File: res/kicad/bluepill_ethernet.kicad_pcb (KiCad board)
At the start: 2 copper layers, 50.4 x 50.4 mm, 47 parts, among them J1 HEADER-1x20, J2 Conn_01x03, J3 Conn_02x05_Odd_Even, J4 HEADER-1x20, J5 Conn_02x02_Odd_Even, J7 Conn_02x04_Odd_Even, SW1 SW_Push, U1 BluePill_STM32F103C, U2 93C46, U3 WIZ850io, U4 93C46, U5 PCF8574A, U6 LM75B

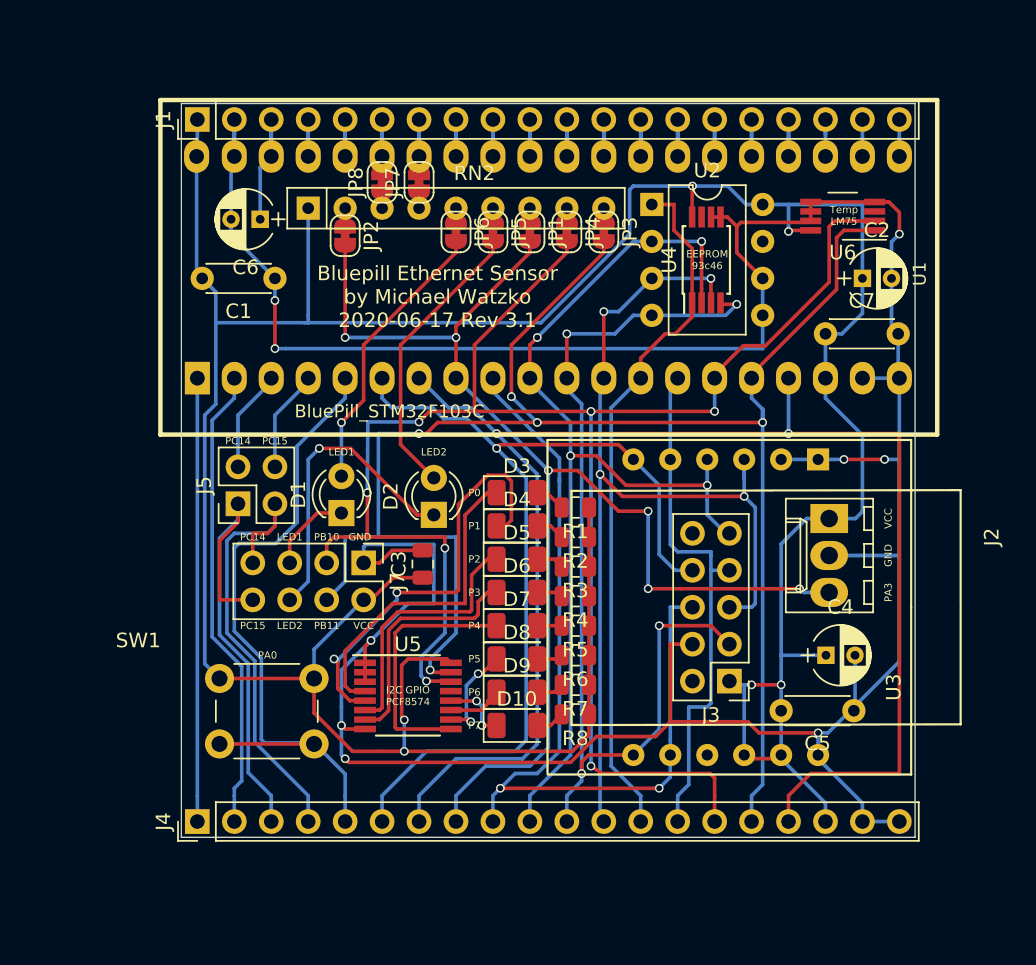
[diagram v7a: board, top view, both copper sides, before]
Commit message: Replace TSSOP packages with SOIC packages
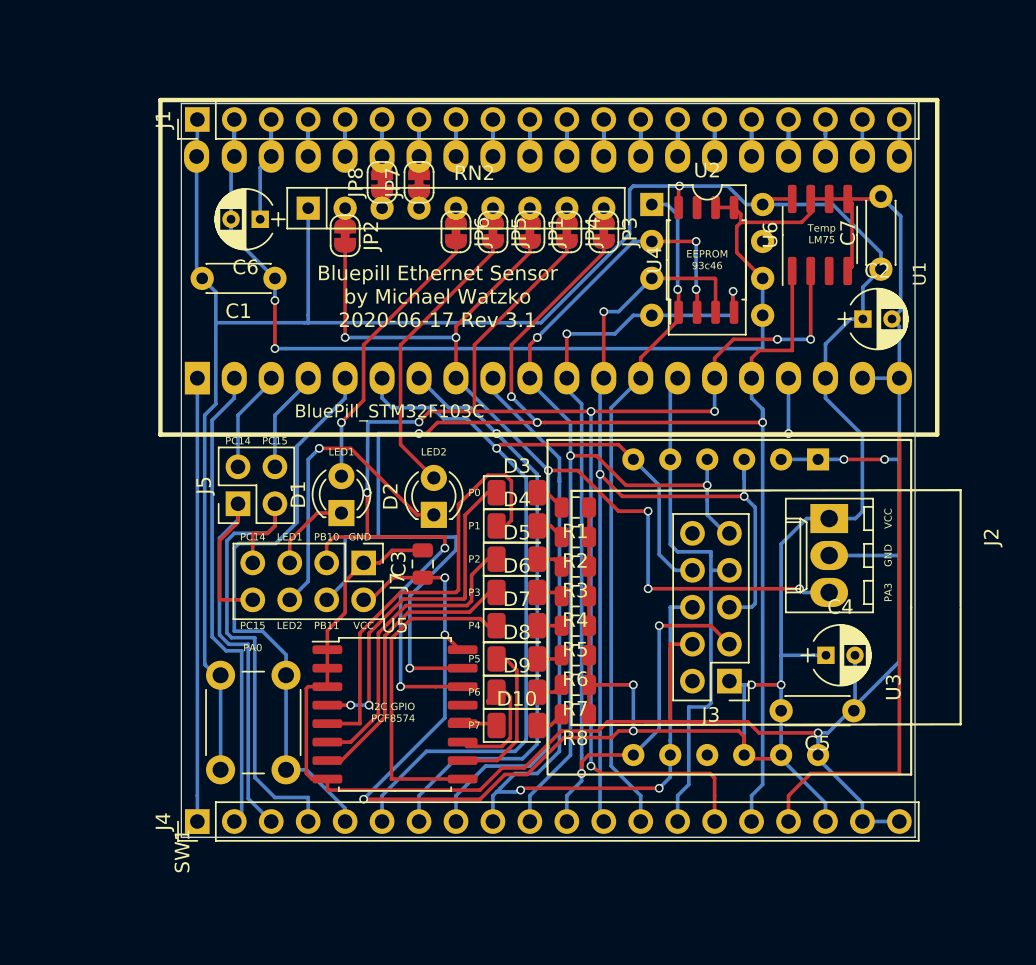
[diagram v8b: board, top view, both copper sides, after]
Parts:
- U4: footprint Housings_SSOP:TSSOP-8_4.4x3mm_Pitch0.65mm -> Package_SO:SOIC-8_5.23x5.23mm_P1.27mm
- U5: footprint Package_SO:TSSOP-16_4.4x5mm_P0.65mm -> Package_SO:SOIC-16W_7.5x10.3mm_P1.27mm
- U6: footprint Package_SO:VSSOP-8_3.0x3.0mm_P0.65mm -> Package_SO:SOIC-8_3.9x4.9mm_P1.27mm
- moved SW1 6.28 mm to (45.5, 76.5), turned to 90 degrees
- moved C7 5.85 mm to (90.9, 42.0), turned to 90 degrees
- moved C2 2.79 mm to (89.7, 45.5)
- moved U6 2.03 mm to (86.7, 39.7), turned to 90 degrees
- moved U5 1.55 mm to (57.5, 72.6)
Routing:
- net VCC: track 235.8 -> 248.8 mm, vias 6 -> 8
- net Net-(J4-Pad5): track 46.8 -> 40.2 mm
- net Net-(D7-Pad1): track 17.6 -> 22.5 mm
- net Net-(D9-Pad1): track 3.75 -> 8.56 mm
- net Net-(D8-Pad1): track 6.91 -> 10.9 mm, vias 2 -> 0
- net Net-(D6-Pad1): track 16.4 -> 19.7 mm
- net Net-(D5-Pad1): track 18.0 -> 21.1 mm
- net GND: track 220.0 -> 217.6 mm, vias 9 -> 5
- net Net-(J4-Pad4): track 32.2 -> 34.4 mm
- net i2c1d: track 120.4 -> 118.2 mm
- net Net-(D3-Pad1): track 22.4 -> 23.9 mm, vias 0 -> 2
- net Net-(J4-Pad13): track 48.0 -> 46.6 mm, vias 0 -> 1
- net Net-(J3-Pad3): track 68.3 -> 69.7 mm
- net i2c1c: track 124.7 -> 123.7 mm, vias 7 -> 9
- net Net-(D4-Pad1): track 29.9 -> 30.8 mm, vias 2 -> 0
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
